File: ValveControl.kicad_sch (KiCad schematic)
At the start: 30 parts, among them J4 Valve_1_PWR, J5 Valve_4_PWR, J6 Valve_2_PWR, J7 Valve_5_PWR, J8 Valve_3_PWR, J9 Valve_6_PWR, Q1 BSS138, Q2 BSS138, Q3 BSS138, Q4 BSS138, Q5 BSS138, Q6 BSS138

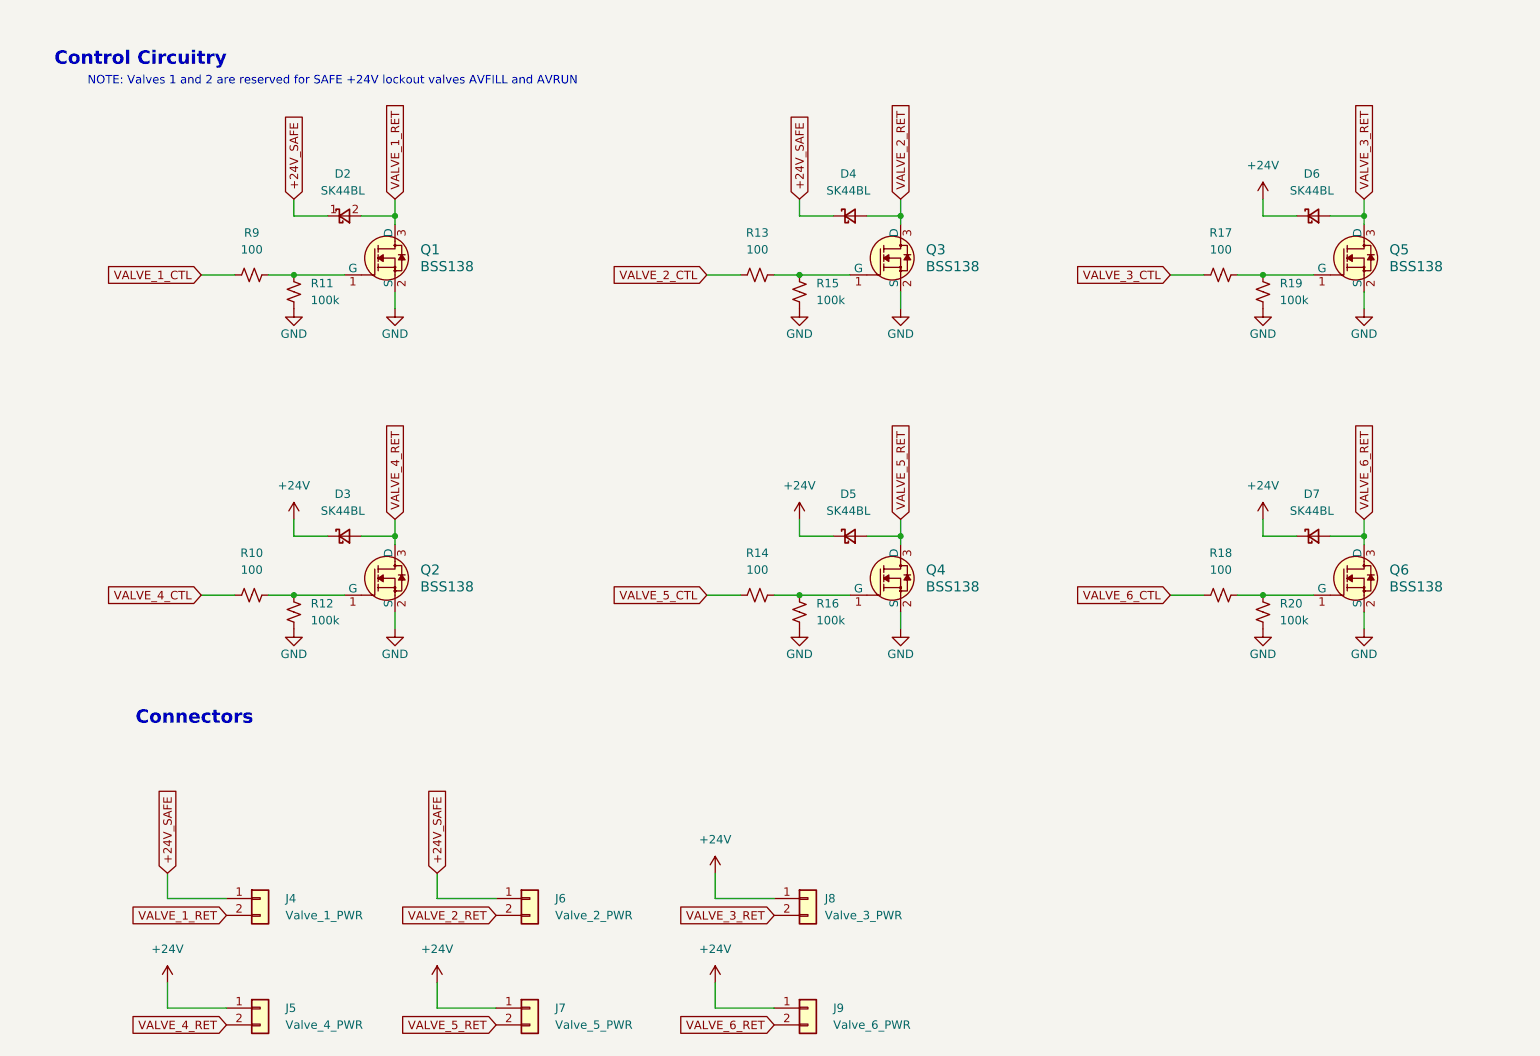
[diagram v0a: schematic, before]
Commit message: revamped schematic to be more readable
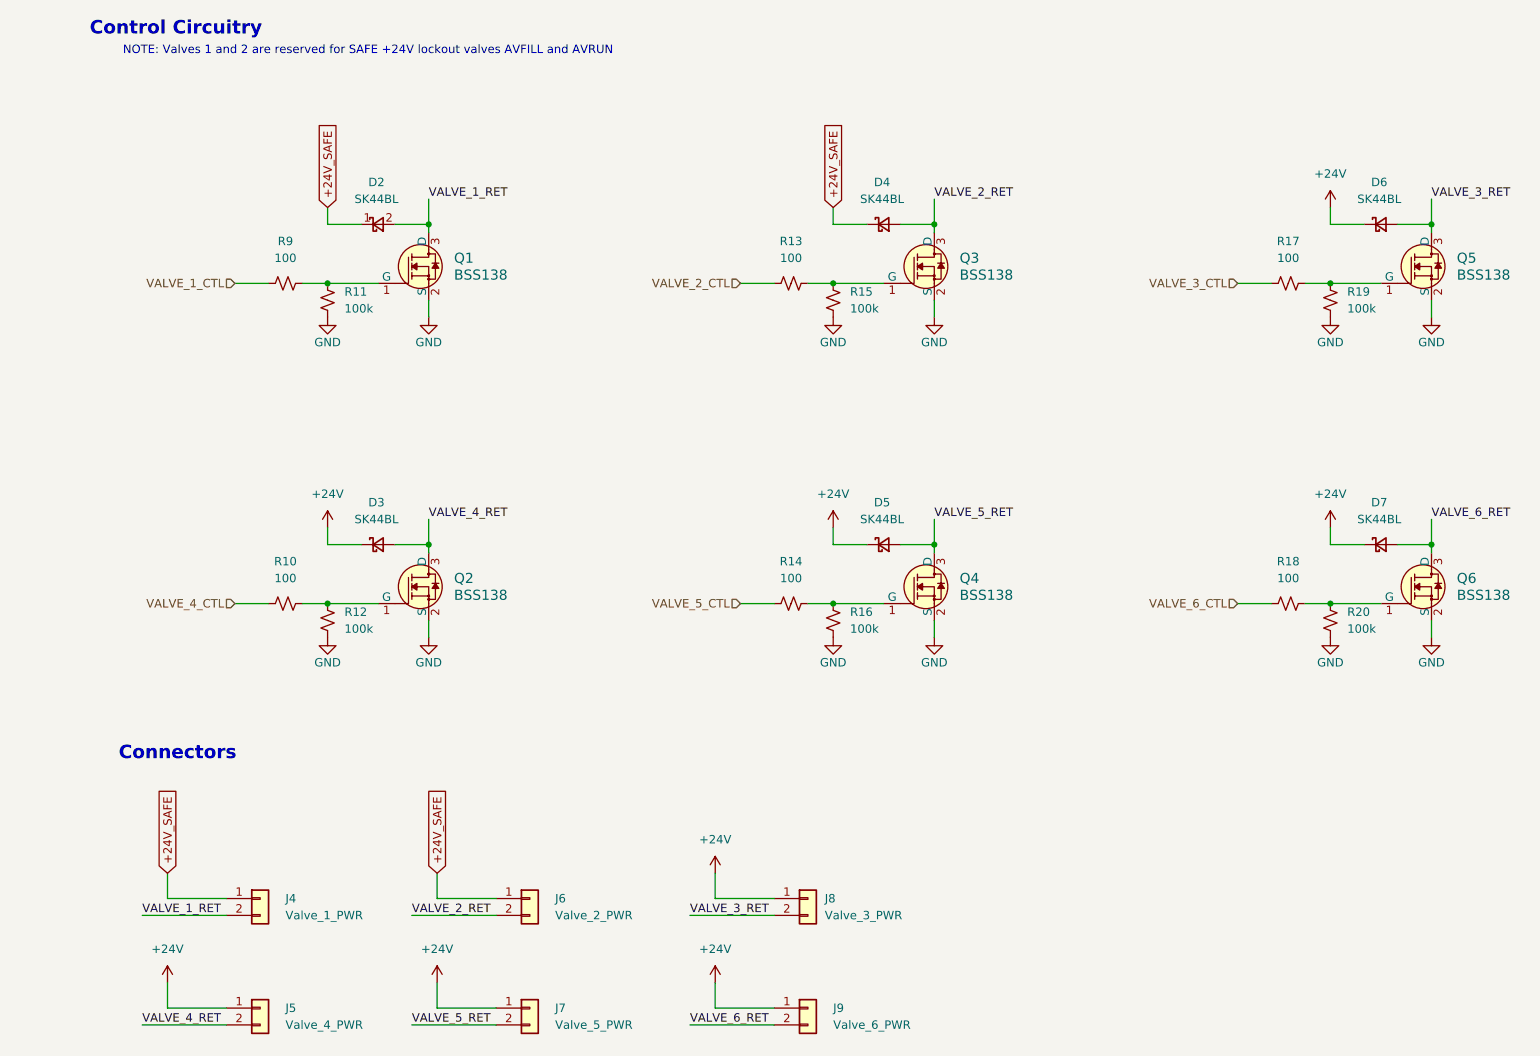
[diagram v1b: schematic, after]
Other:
- moved on the sheet: D2, D3, D4, D5, D6, D7, Q1, Q2, Q3, Q4, Q5, Q6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

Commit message: add 2 stage lockout to ignitor, add ignitor resistance reading with adc current source
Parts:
- renumbered D2 to D32, D3 to D33, D4 to D34, D5 to D35, D6 to D36, D7 to D37, J4 to J15, J5 to J16, J6 to J17, J7 to J18, J8 to J19, J9 to J20, Q5 to Q10, Q6 to Q11, Q1 to Q6, Q2 to Q7, Q3 to Q8, Q4 to Q9, R9 to R78, R10 to R79, R11 to R80, R12 to R81, R13 to R82, R14 to R83, R15 to R84, R16 to R85, R17 to R86, R18 to R87, R19 to R88, R20 to R89

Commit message: add capacitor and resistor footprints
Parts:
- R84: renamed from R80; footprint Resistor_SMD:R_0402_1005Metric -> Resistor_SMD:R_0603_1608Metric
- R85: renamed from R81; footprint Resistor_SMD:R_0402_1005Metric -> Resistor_SMD:R_0603_1608Metric
- R88: renamed from R84; footprint Resistor_SMD:R_0402_1005Metric -> Resistor_SMD:R_0603_1608Metric
- R89: renamed from R85; footprint Resistor_SMD:R_0402_1005Metric -> Resistor_SMD:R_0603_1608Metric
- R92: renamed from R88; footprint Resistor_SMD:R_0402_1005Metric -> Resistor_SMD:R_0603_1608Metric
- R93: renamed from R89; footprint Resistor_SMD:R_0402_1005Metric -> Resistor_SMD:R_0603_1608Metric
- renumbered D32 to D28, D33 to D29, D34 to D30, D35 to D31, D36 to D32, D37 to D33, J15 to J14, J16 to J15, J17 to J16, J18 to J17, J19 to J18, J20 to J19, R78 to R82, R79 to R83, R82 to R86, R83 to R87, R86 to R90, R87 to R91

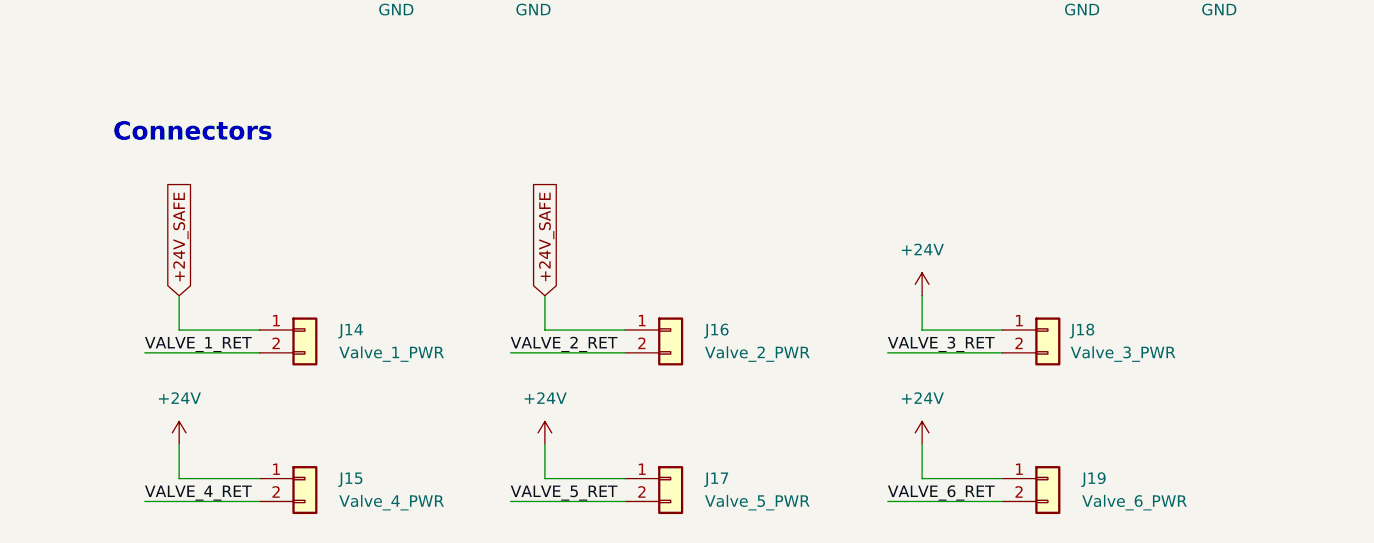
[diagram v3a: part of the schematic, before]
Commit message: change connectors and more progress on pcb
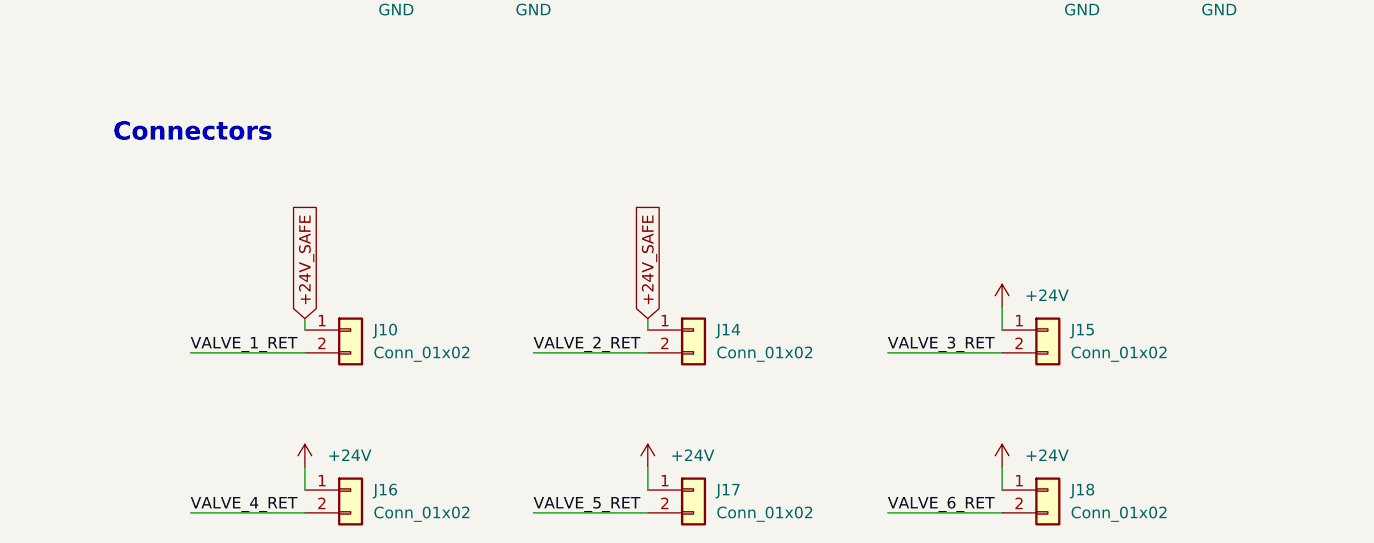
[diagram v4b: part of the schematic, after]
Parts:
- removed J19: Valve_6_PWR, Connector_JST:JST_XH_B2B-XH-A_1x02_P2.50mm_Vertical, symbol Connector_Generic:Conn_01x02
- added J10: Conn_01x02, Connector_Molex:Molex_Micro-Fit_3.0_43650-0215_1x02_P3.00mm_Vertical, symbol Connector_Generic:Conn_01x02
- J14: value Valve_1_PWR -> Conn_01x02; footprint Connector_JST:JST_XH_B2B-XH-A_1x02_P2.50mm_Vertical -> Connector_Molex:Molex_Micro-Fit_3.0_43650-0215_1x02_P3.00mm_Vertical; LCSC C20079 -> (none); MPN XH-2A -> (none); now in the parts list
- J15: value Valve_4_PWR -> Conn_01x02; footprint Connector_JST:JST_XH_B2B-XH-A_1x02_P2.50mm_Vertical -> Connector_Molex:Molex_Micro-Fit_3.0_43650-0215_1x02_P3.00mm_Vertical; LCSC C20079 -> (none); MPN XH-2A -> (none); now in the parts list
- J16: value Valve_2_PWR -> Conn_01x02; footprint Connector_JST:JST_XH_B2B-XH-A_1x02_P2.50mm_Vertical -> Connector_Molex:Molex_Micro-Fit_3.0_43650-0215_1x02_P3.00mm_Vertical; LCSC C20079 -> (none); MPN XH-2A -> (none); now in the parts list
- J17: value Valve_5_PWR -> Conn_01x02; footprint Connector_JST:JST_XH_B2B-XH-A_1x02_P2.50mm_Vertical -> Connector_Molex:Molex_Micro-Fit_3.0_43650-0215_1x02_P3.00mm_Vertical; LCSC C20079 -> (none); MPN XH-2A -> (none); now in the parts list
- J18: value Valve_3_PWR -> Conn_01x02; footprint Connector_JST:JST_XH_B2B-XH-A_1x02_P2.50mm_Vertical -> Connector_Molex:Molex_Micro-Fit_3.0_43650-0215_1x02_P3.00mm_Vertical; LCSC C20079 -> (none); MPN XH-2A -> (none); now in the parts list
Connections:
- net +24V: now also J16.1 (Pin_1)
- net +24V_SAFE: now also J10.1 (Pin_1); no longer J16.1 (Pin_1)
- net VALVE_1_RET: now also J10.2 (Pin_2); no longer J14.2 (Pin_2)
- net VALVE_2_RET: now also J14.2 (Pin_2); no longer J16.2 (Pin_2)
- net VALVE_3_RET: now also J15.2 (Pin_2); no longer J18.2 (Pin_2)
- net VALVE_4_RET: now also J16.2 (Pin_2); no longer J15.2 (Pin_2)
- net VALVE_6_RET: now also J18.2 (Pin_2)

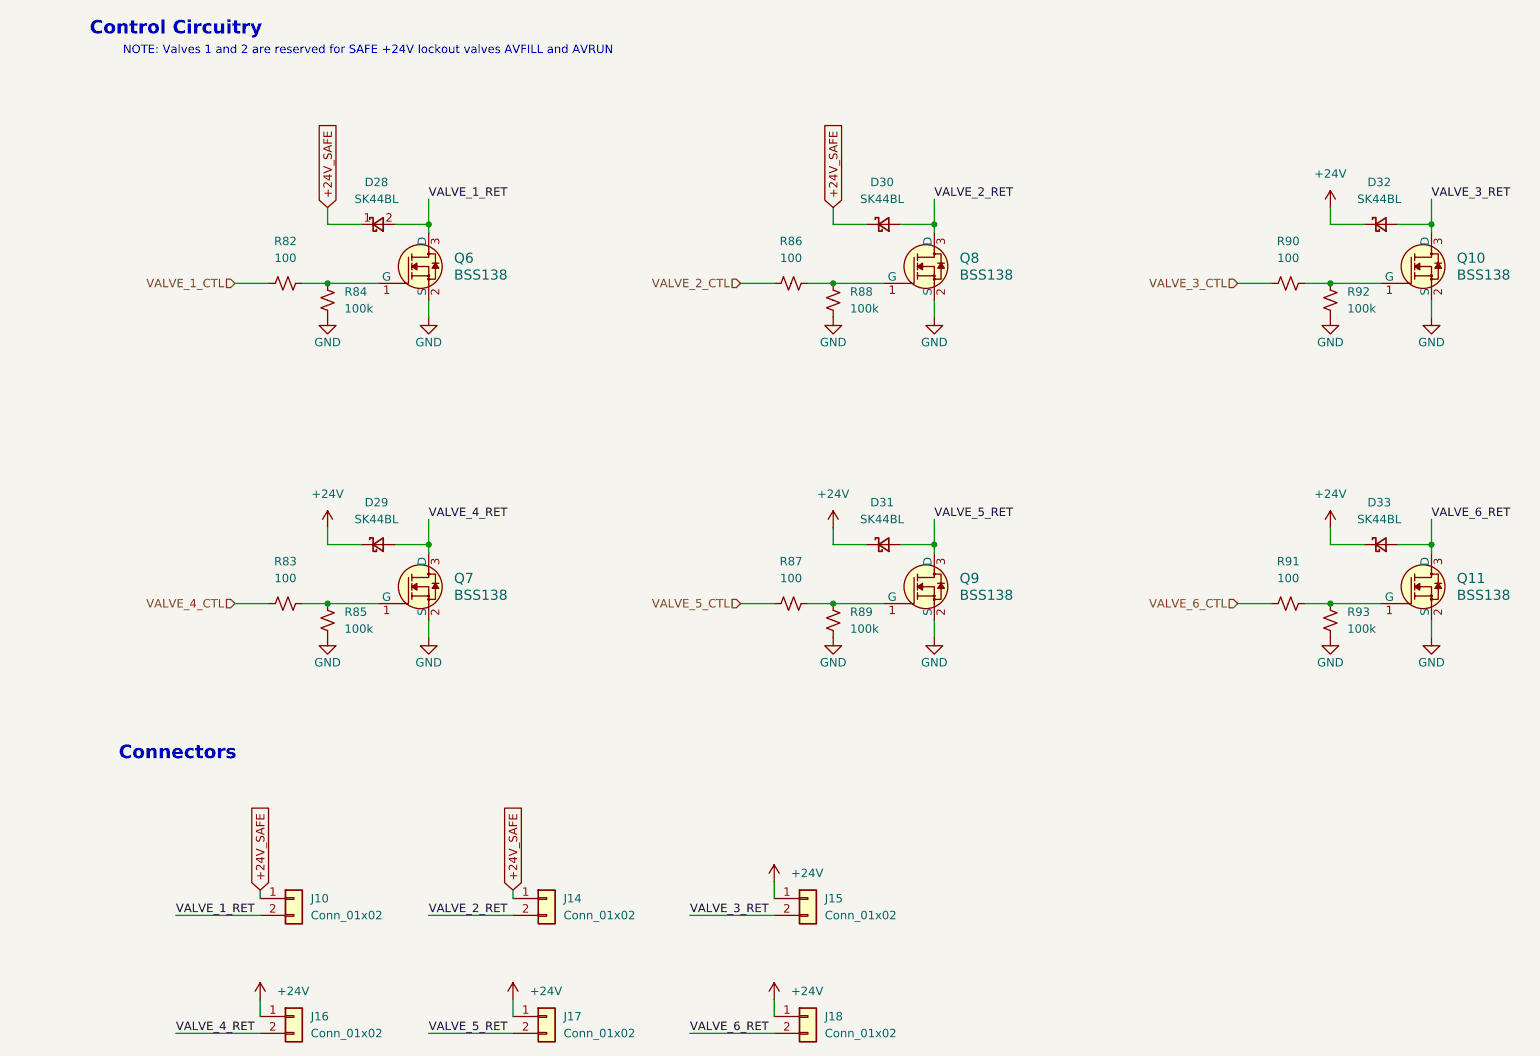
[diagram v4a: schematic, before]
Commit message: change clamping resistors on tc adcs for lower leakage current
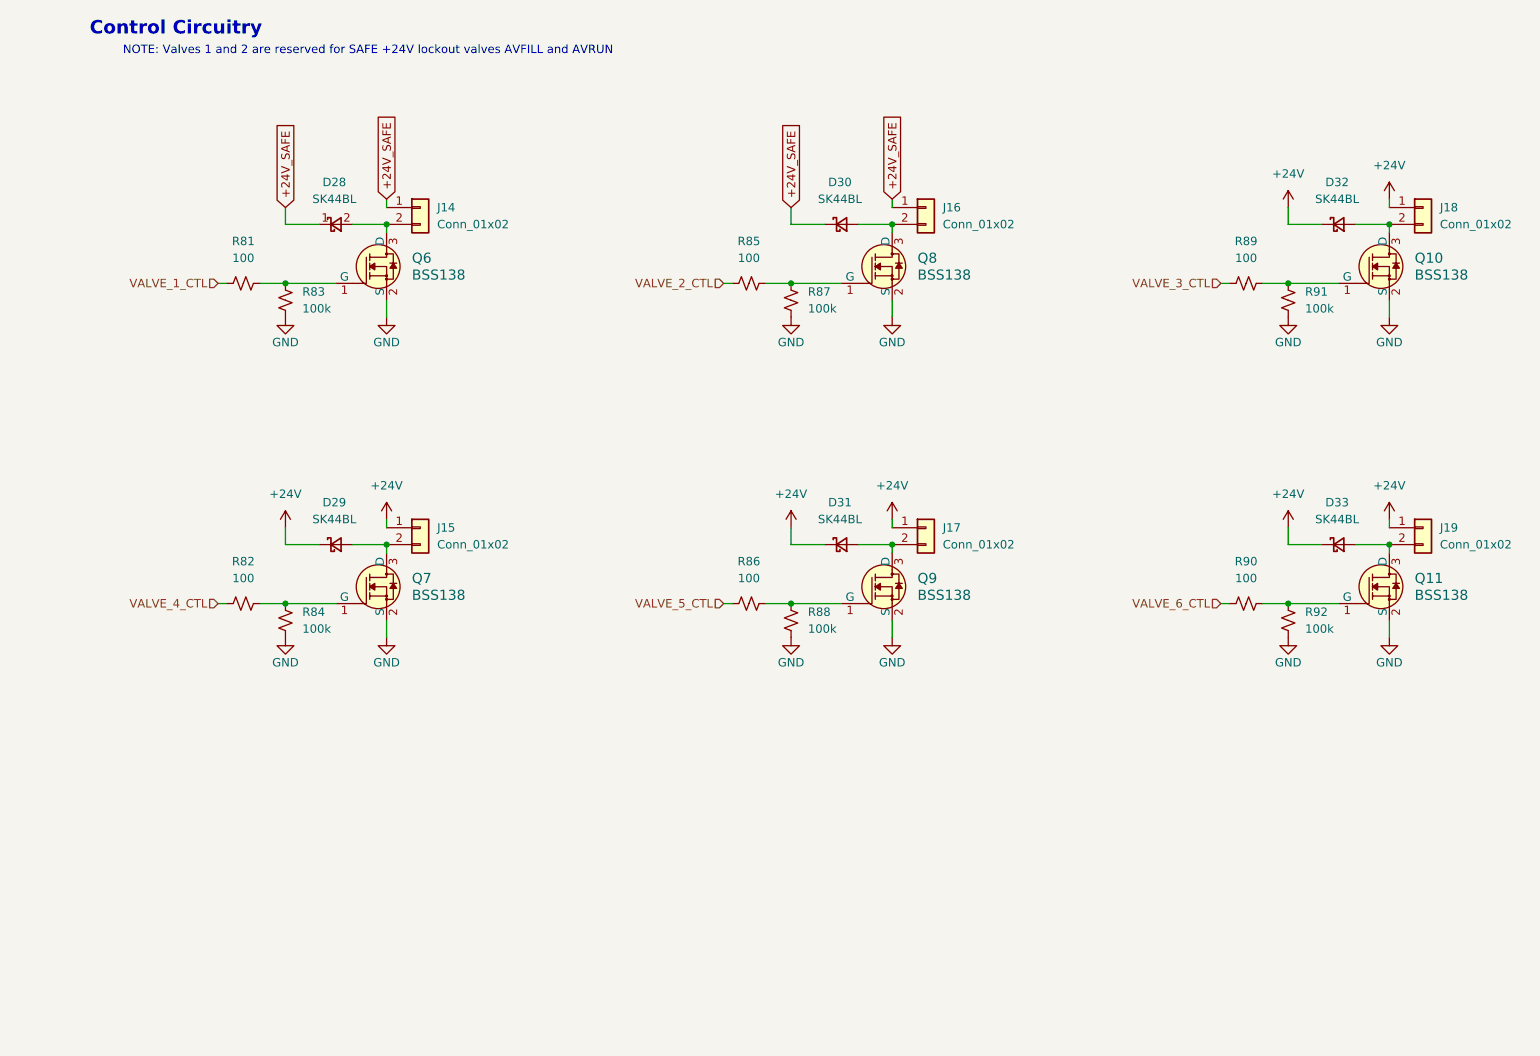
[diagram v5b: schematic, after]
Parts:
- removed J14: Conn_01x02, Connector_Molex:Molex_Micro-Fit_3.0_43650-0215_1x02_P3.00mm_Vertical, symbol Connector_Generic:Conn_01x02
- added J19: Conn_01x02, Connector_Molex:Molex_Micro-Fit_3.0_43650-0215_1x02_P3.00mm_Vertical, symbol Connector_Generic:Conn_01x02
- renumbered J10 to J14, R82 to R81, R83 to R82, R84 to R83, R85 to R84, R86 to R85, R87 to R86, R88 to R87, R89 to R88, R90 to R89, R91 to R90, R92 to R91, R93 to R92
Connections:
- net +24V: now also J19.1 (Pin_1); no longer J16.1 (Pin_1)
- net +24V_SAFE: now also J16.1 (Pin_1)
- net VALVE_1_RET: no longer names the net of D28.2 (A), J14.2 (Pin_2), Q6.3 (D)
- net VALVE_2_RET: no longer names the net of D30.2 (A), Q8.3 (D)
- net VALVE_2_RET: now also J16.2 (Pin_2)
- net VALVE_3_RET: no longer names the net of D32.2 (A), Q10.3 (D)
- net VALVE_3_RET: now also J18.2 (Pin_2); no longer J15.2 (Pin_2)
- net VALVE_4_RET: no longer names the net of D29.2 (A), Q7.3 (D)
- net VALVE_4_RET: now also J15.2 (Pin_2); no longer J16.2 (Pin_2)
- net VALVE_5_RET: no longer names the net of D31.2 (A), J17.2 (Pin_2), Q9.3 (D)
- net VALVE_6_RET: no longer names the net of D33.2 (A), Q11.3 (D)
- net VALVE_6_RET: now also J19.2 (Pin_2); no longer J18.2 (Pin_2)
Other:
- note removed: "Connectors"
- moved on the sheet: D28, D29, D30, D31, D32, D33, J14, Q10, Q11, Q6, Q7, Q8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

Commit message: Update version number in KiCad files
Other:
- title: Valve Control -> PANDA
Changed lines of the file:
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@@
 	(paper "A4")
 	(title_block
-		(title "Valve Control")
-		(rev "1.0.0")
+		(title "PANDA")
+		(date "2025-12-21")
+		(rev "3.0.0")
 		(company "Queen's Rocket Engineering Team")
 	)
@@
 		(polyline
 			(pts
-				(xy 105.41 81.28) (xy 168.91 81.28) (xy 168.91 120.65) (xy 105.41 120.65)
+				(xy 29.21 81.28) (xy 92.71 81.28) (xy 92.71 120.65) (xy 29.21 120.65)
+			)
+			(stroke
+				(width 0)
+				(type dash)
+			)
+			(fill
+				(type none)
+			)
+		)
+	)
+	(rule_area
+		(polyline
+			(pts
+				(xy 29.21 33.02) (xy 92.71 33.02) (xy 92.71 72.39) (xy 29.21 72.39)
+			)
+			(stroke
+				(width 0)
+				(type dash)
+			)
+			(fill
+				(type none)
+			)
+		)
+	)
+	(rule_area
+		(polyline
+			(pts
+				(xy 179.07 33.02) (xy 242.57 33.02) (xy 242.57 72.39) (xy 179.07 72.39)
 			)
 			(stroke
@@
 		(polyline
 			(pts
-				(xy 29.21 81.28) (xy 92.71 81.28) (xy 92.71 120.65) (xy 29.21 120.65)
+				(xy 179.07 81.28) (xy 242.57 81.28) (xy 242.57 120.65) (xy 179.07 120.65)
 			)
 			(stroke
@@
 		(polyline
 			(pts
-				(xy 29.21 33.02) (xy 92.71 33.02) (xy 92.71 72.39) (xy 29.21 72.39)
+				(xy 105.41 81.28) (xy 168.91 81.28) (xy 168.91 120.65) (xy 105.41 120.65)
 			)
 			(stroke
-				(width 0)
-				(type dash)
-			)
-			(fill
-				(type none)
-			)
-		)
-	)
-	(rule_area
-		(polyline
-			(pts
-				(xy 179.07 81.28) (xy 242.57 81.28) (xy 242.57 120.65) (xy 179.07 120.65)
-			)
-			(stroke
-				(width 0)
-				(type dash)
-			)
-			(fill
-				(type none)
-			)
-		)
-	)
-	(rule_area
-		(polyline
-			(pts
-				(xy 179.07 33.02) (xy 242.57 33.02) (xy 242.57 72.39) (xy 179.07 72.39)
-			)
-			(stroke
